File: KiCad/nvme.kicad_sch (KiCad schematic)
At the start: 35 parts, among them J10 Bus_M.2_Socket_M, J11 Bus_M.2_Socket_M, J12 Bus_M.2_Socket_M, J13 Bus_M.2_Socket_M, J14 Bus_M.2_Socket_M

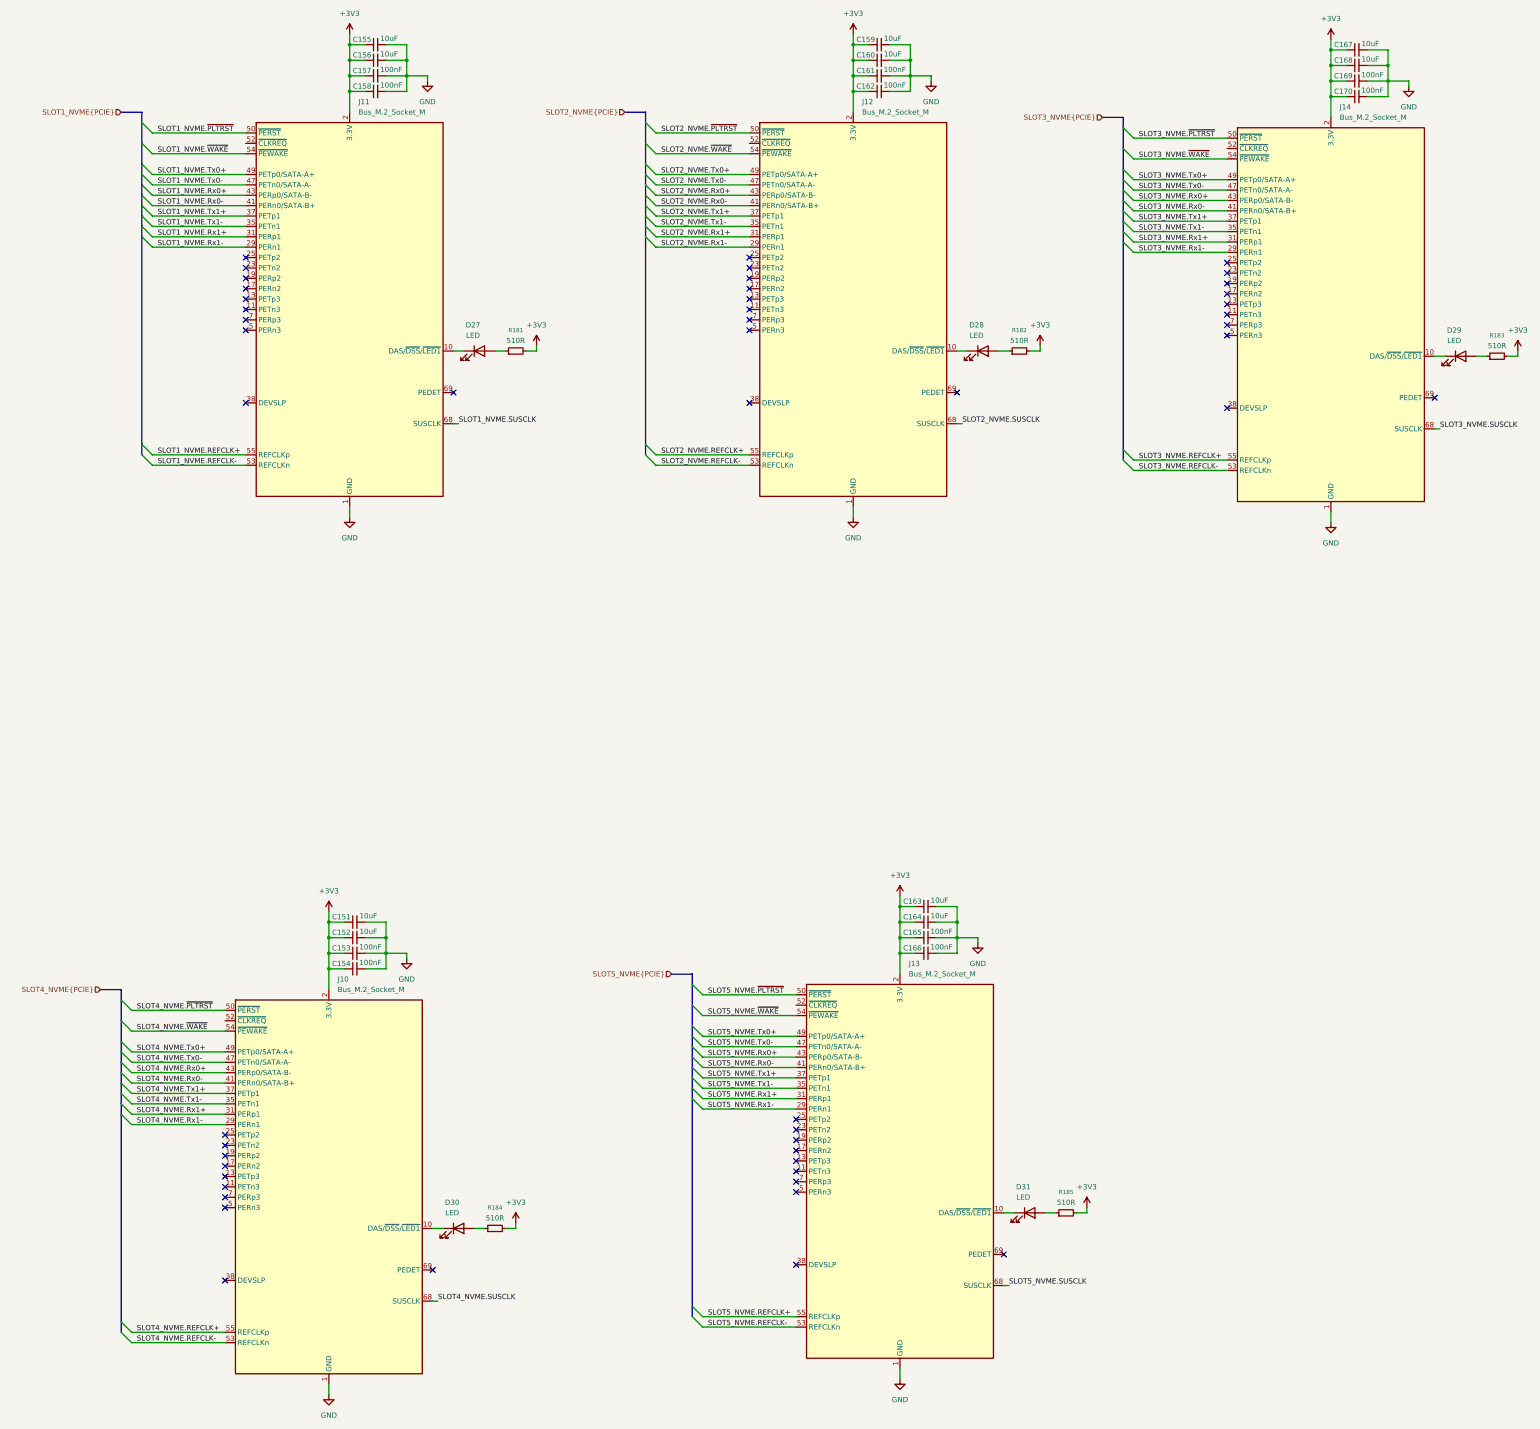
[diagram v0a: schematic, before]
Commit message: Remove 0.95V Power Supply, Replace 3.3V Standby Power Supply
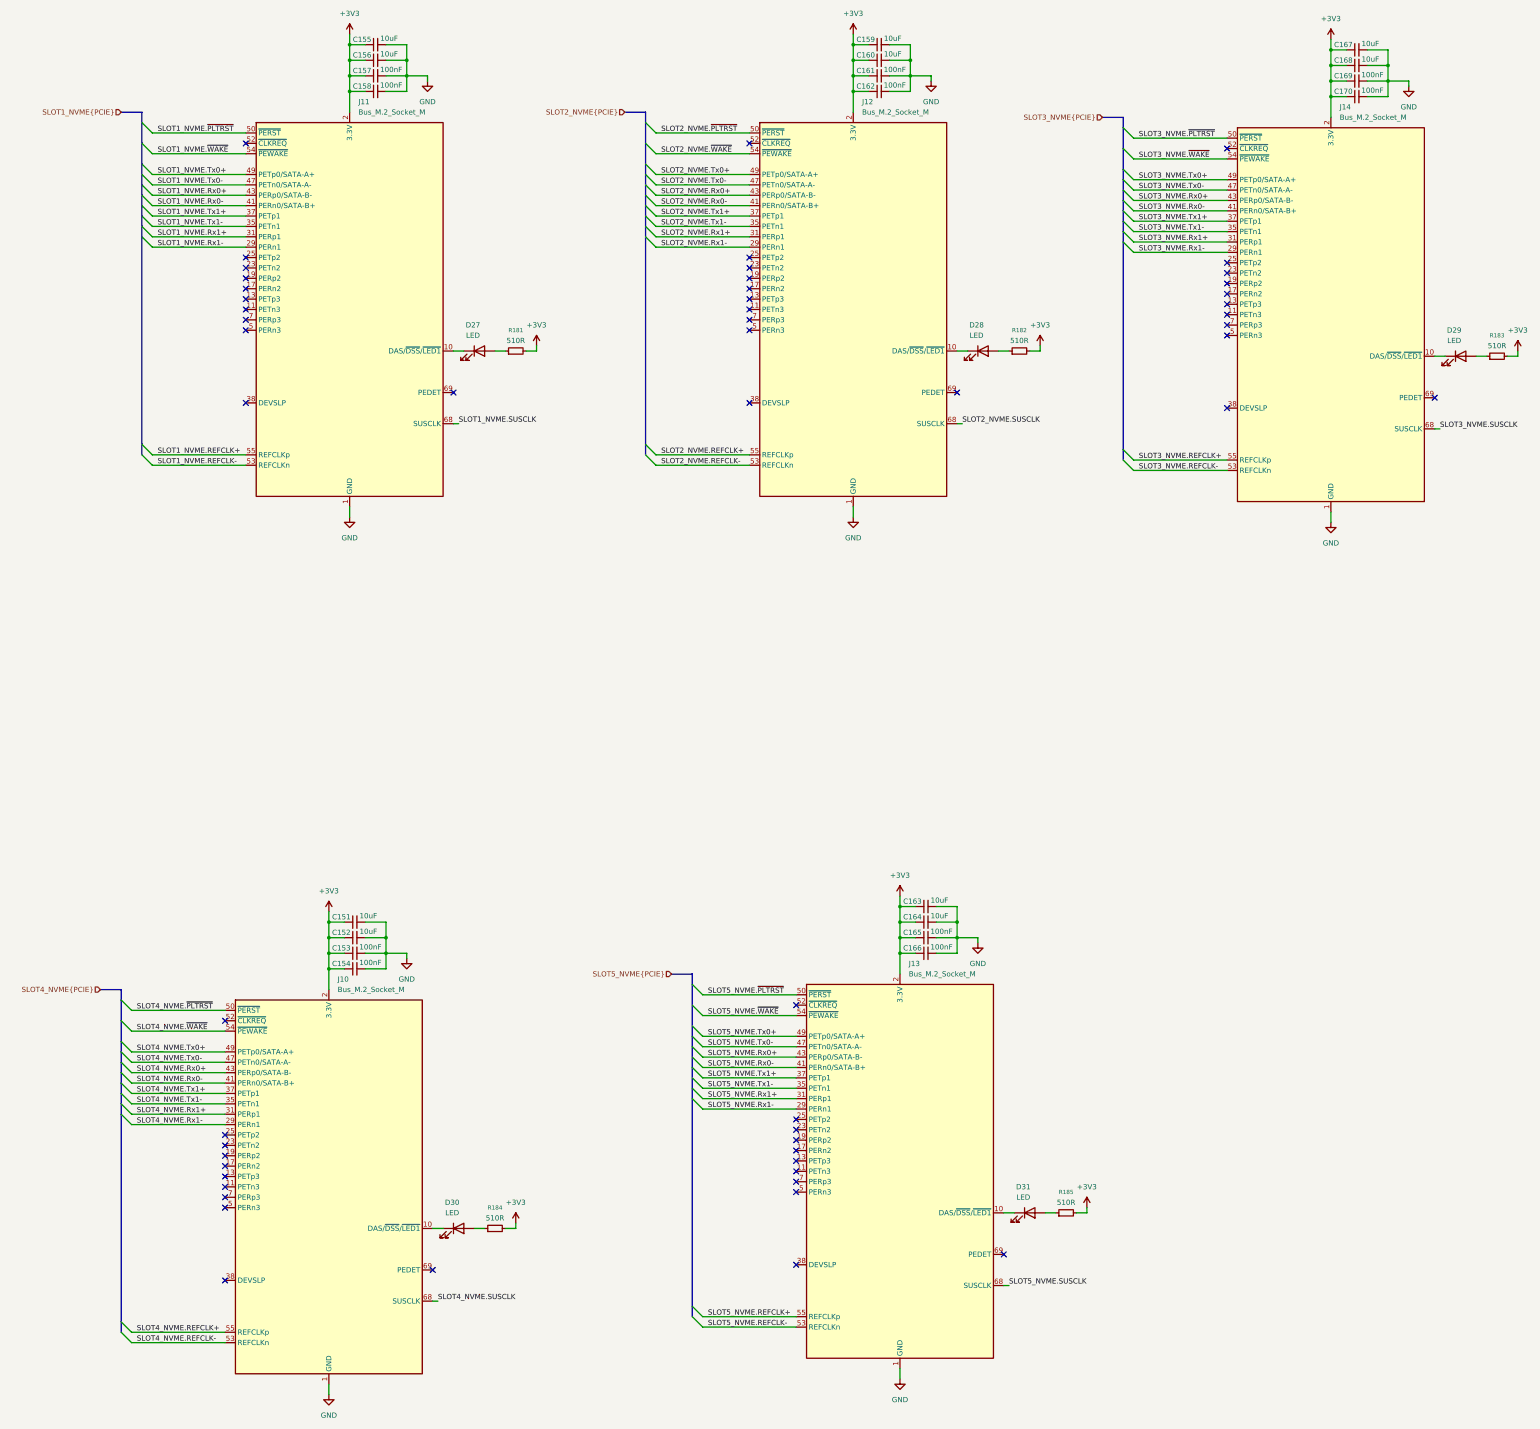
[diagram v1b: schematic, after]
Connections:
- no-connect marks 50 -> 55
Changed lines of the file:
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@@
+	)
+	(no_connect
+		(at 132.08 60.96)
 	)
 	(no_connect
@@
 	(no_connect
 		(at 127 321.31)
+	)
+	(no_connect
+		(at 255.27 60.96)
 	)
 	(no_connect
@@
 	(no_connect
 		(at 132.08 101.6)
+	)
+	(no_connect
+		(at 266.7 271.78)
 	)
 	(no_connect
@@
 	)
 	(no_connect
+		(at 372.11 62.23)
+	)
+	(no_connect
 		(at 255.27 106.68)
 	)
@@
 	)
 	(no_connect
+		(at 127 275.59)
+	)
+	(no_connect

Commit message: Work though ERC errors
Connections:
- net SLOT2_NVME.REFCLK+: now also J10.55 (REFCLKp); no longer J12.55 (REFCLKp)
- net SLOT2_NVME.REFCLK-: now also J10.53 (REFCLKn); no longer J12.53 (REFCLKn)
- net SLOT2_NVME.Rx0+: now also J10.43 (PERp0/SATA-B-); no longer J12.43 (PERp0/SATA-B-)
- net SLOT2_NVME.Rx0-: now also J10.41 (PERn0/SATA-B+); no longer J12.41 (PERn0/SATA-B+)
- net SLOT2_NVME.Rx1+: now also J10.31 (PERp1); no longer J12.31 (PERp1)
- net SLOT2_NVME.Rx1-: now also J10.29 (PERn1); no longer J12.29 (PERn1)
- net SLOT2_NVME.SUSCLK: now also J10.68 (SUSCLK); no longer J12.68 (SUSCLK)
- net SLOT2_NVME.Tx0+: now also J10.49 (PETp0/SATA-A+); no longer J12.49 (PETp0/SATA-A+)
- net SLOT2_NVME.Tx0-: now also J10.47 (PETn0/SATA-A-); no longer J12.47 (PETn0/SATA-A-)
- net SLOT2_NVME.Tx1+: now also J10.37 (PETp1); no longer J12.37 (PETp1)
- net SLOT2_NVME.Tx1-: now also J10.35 (PETn1); no longer J12.35 (PETn1)
- net SLOT2_NVME.~{PLTRST}: now also J10.50 (~{PERST}); no longer J12.50 (~{PERST})
- net SLOT2_NVME.~{WAKE}: now also J10.54 (~{PEWAKE}); no longer J12.54 (~{PEWAKE})
- net SLOT3_NVME.REFCLK+: now also J12.55 (REFCLKp); no longer J14.55 (REFCLKp)
- net SLOT3_NVME.REFCLK-: now also J12.53 (REFCLKn); no longer J14.53 (REFCLKn)
- net SLOT3_NVME.Rx0+: now also J12.43 (PERp0/SATA-B-); no longer J14.43 (PERp0/SATA-B-)
- net SLOT3_NVME.Rx0-: now also J12.41 (PERn0/SATA-B+); no longer J14.41 (PERn0/SATA-B+)
- net SLOT3_NVME.Rx1+: now also J12.31 (PERp1); no longer J14.31 (PERp1)
- net SLOT3_NVME.Rx1-: now also J12.29 (PERn1); no longer J14.29 (PERn1)
- net SLOT3_NVME.SUSCLK: now also J12.68 (SUSCLK); no longer J14.68 (SUSCLK)
- net SLOT3_NVME.Tx0+: now also J12.49 (PETp0/SATA-A+); no longer J14.49 (PETp0/SATA-A+)
- net SLOT3_NVME.Tx0-: now also J12.47 (PETn0/SATA-A-); no longer J14.47 (PETn0/SATA-A-)
- net SLOT3_NVME.Tx1+: now also J12.37 (PETp1); no longer J14.37 (PETp1)
- net SLOT3_NVME.Tx1-: now also J12.35 (PETn1); no longer J14.35 (PETn1)
- net SLOT3_NVME.~{PLTRST}: now also J12.50 (~{PERST}); no longer J14.50 (~{PERST})
- net SLOT3_NVME.~{WAKE}: now also J12.54 (~{PEWAKE}); no longer J14.54 (~{PEWAKE})
- net SLOT4_NVME.REFCLK+: now also J13.55 (REFCLKp); no longer J10.55 (REFCLKp)
- net SLOT4_NVME.REFCLK-: now also J13.53 (REFCLKn); no longer J10.53 (REFCLKn)
- net SLOT4_NVME.Rx0+: now also J13.43 (PERp0/SATA-B-); no longer J10.43 (PERp0/SATA-B-)
- net SLOT4_NVME.Rx0-: now also J13.41 (PERn0/SATA-B+); no longer J10.41 (PERn0/SATA-B+)
- net SLOT4_NVME.Rx1+: now also J13.31 (PERp1); no longer J10.31 (PERp1)
- net SLOT4_NVME.Rx1-: now also J13.29 (PERn1); no longer J10.29 (PERn1)
- net SLOT4_NVME.SUSCLK: now also J13.68 (SUSCLK); no longer J10.68 (SUSCLK)
- net SLOT4_NVME.Tx0+: now also J13.49 (PETp0/SATA-A+); no longer J10.49 (PETp0/SATA-A+)
- net SLOT4_NVME.Tx0-: now also J13.47 (PETn0/SATA-A-); no longer J10.47 (PETn0/SATA-A-)
- net SLOT4_NVME.Tx1+: now also J13.37 (PETp1); no longer J10.37 (PETp1)
- net SLOT4_NVME.Tx1-: now also J13.35 (PETn1); no longer J10.35 (PETn1)
- net SLOT4_NVME.~{PLTRST}: now also J13.50 (~{PERST}); no longer J10.50 (~{PERST})
- net SLOT4_NVME.~{WAKE}: now also J13.54 (~{PEWAKE}); no longer J10.54 (~{PEWAKE})
- net SLOT5_NVME.REFCLK+: now also J14.55 (REFCLKp); no longer J13.55 (REFCLKp)
- net SLOT5_NVME.REFCLK-: now also J14.53 (REFCLKn); no longer J13.53 (REFCLKn)
- net SLOT5_NVME.Rx0+: now also J14.43 (PERp0/SATA-B-); no longer J13.43 (PERp0/SATA-B-)
- net SLOT5_NVME.Rx0-: now also J14.41 (PERn0/SATA-B+); no longer J13.41 (PERn0/SATA-B+)
- net SLOT5_NVME.Rx1+: now also J14.31 (PERp1); no longer J13.31 (PERp1)
- net SLOT5_NVME.Rx1-: now also J14.29 (PERn1); no longer J13.29 (PERn1)
- net SLOT5_NVME.SUSCLK: now also J14.68 (SUSCLK); no longer J13.68 (SUSCLK)
- net SLOT5_NVME.Tx0+: now also J14.49 (PETp0/SATA-A+); no longer J13.49 (PETp0/SATA-A+)
- net SLOT5_NVME.Tx0-: now also J14.47 (PETn0/SATA-A-); no longer J13.47 (PETn0/SATA-A-)
- net SLOT5_NVME.Tx1+: now also J14.37 (PETp1); no longer J13.37 (PETp1)
- net SLOT5_NVME.Tx1-: now also J14.35 (PETn1); no longer J13.35 (PETn1)
- net SLOT5_NVME.~{PLTRST}: now also J14.50 (~{PERST}); no longer J13.50 (~{PERST})
- net SLOT5_NVME.~{WAKE}: now also J14.54 (~{PEWAKE}); no longer J13.54 (~{PEWAKE})
- net at D29.1 (K): now also J12.10 (DAS/~{DSS}/~{LED1}); no longer J14.10 (DAS/~{DSS}/~{LED1})
- net at D30.1 (K): now also J13.10 (DAS/~{DSS}/~{LED1}); no longer J10.10 (DAS/~{DSS}/~{LED1})
- net at D28.1 (K): now also J10.10 (DAS/~{DSS}/~{LED1}); no longer J12.10 (DAS/~{DSS}/~{LED1})
- net at D31.1 (K): now also J14.10 (DAS/~{DSS}/~{LED1}); no longer J13.10 (DAS/~{DSS}/~{LED1})

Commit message: Re-annotate components
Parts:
- renumbered C151 to C163, C152 to C164, C153 to C165, C154 to C166, C155 to C167, C156 to C168, C157 to C169, C158 to C170, C159 to C171, C160 to C172, C161 to C173, C162 to C174, C163 to C175, C164 to C176, C165 to C177, C166 to C178, C167 to C179, C168 to C180, C169 to C181, C170 to C182, D30 to D22, D27 to D23, D28 to D24, D31 to D25, D29 to D26, J13 to J10, J10 to J12, J14 to J13, J12 to J14, R184 to R108, R181 to R109, R182 to R110, R185 to R111, R183 to R112

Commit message: Add more footprints
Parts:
- C163, C164, C165, C166, C167, C168, C169, C170, C171, C172, C173, C174, C175, C176, C177, C178, C179, C180, C181, C182: footprint (none) -> Capacitor_SMD:C_0603_1608Metric
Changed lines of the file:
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@@
 			)
 		)
-		(property "Footprint" ""
+		(property "Footprint" "Capacitor_SMD:C_0603_1608Metric"
 			(at 298.45 259.08 0)
 			(effects
@@
 			)
 		)
-		(property "Footprint" ""
+		(property "Footprint" "Capacitor_SMD:C_0603_1608Metric"
 			(at 158.75 259.08 0)
 			(effects
@@
 			)
 		)
-		(property "Footprint" ""
+		(property "Footprint" "Capacitor_SMD:C_0603_1608Metric"
 			(at 158.75 255.27 0)
 			(effects
@@
 			)
 		)
-		(property "Footprint" ""
+		(property "Footprint" "Capacitor_SMD:C_0603_1608Metric"
 			(at 403.86 38.1 0)
 			(effects
@@
 			)
 		)
-		(property "Footprint" ""
+		(property "Footprint" "Capacitor_SMD:C_0603_1608Metric"
 			(at 287.02 48.26 0)
 			(effects
@@
 			)
 		)
-		(property "Footprint" ""
+		(property "Footprint" "Capacitor_SMD:C_0603_1608Metric"
 			(at 163.83 36.83 0)
 			(effects
@@
 			)
 		)
-		(property "Footprint" ""
+		(property "Footprint" "Capacitor_SMD:C_0603_1608Metric"
 			(at 158.75 251.46 0)
 			(effects
@@
 			)
 		)
-		(property "Footprint" ""
+		(property "Footprint" "Capacitor_SMD:C_0603_1608Metric"
 			(at 163.83 48.26 0)
 			(effects
@@
 			)
 		)
-		(property "Footprint" ""
+		(property "Footprint" "Capacitor_SMD:C_0603_1608Metric"
 			(at 298.45 255.27 0)
 			(effects
@@
 			)
 		)
-		(property "Footprint" ""
+		(property "Footprint" "Capacitor_SMD:C_0603_1608Metric"
 			(at 287.02 36.83 0)
 			(effects
@@
 			)
 		)
-		(property "Footprint" ""
+		(property "Footprint" "Capacitor_SMD:C_0603_1608Metric"
 			(at 163.83 44.45 0)
 			(effects
@@
 			)
 		)
-		(property "Footprint" ""
+		(property "Footprint" "Capacitor_SMD:C_0603_1608Metric"
 			(at 287.02 44.45 0)
 			(effects
@@
 			)
 		)
-		(property "Footprint" ""
+		(property "Footprint" "Capacitor_SMD:C_0603_1608Metric"
 			(at 403.86 49.53 0)
 			(effects
@@
 			)
 		)
-		(property "Footprint" ""
+		(property "Footprint" "Capacitor_SMD:C_0603_1608Metric"
 			(at 403.86 41.91 0)
 			(effects
@@
 			)
 		)
-		(property "Footprint" ""
+		(property "Footprint" "Capacitor_SMD:C_0603_1608Metric"
 			(at 298.45 251.46 0)
 			(effects
@@
 			)
 		)
-		(property "Footprint" ""
+		(property "Footprint" "Capacitor_SMD:C_0603_1608Metric"
 			(at 403.86 45.72 0)
 			(effects
@@
 			)
 		)
-		(property "Footprint" ""
+		(property "Footprint" "Capacitor_SMD:C_0603_1608Metric"
 			(at 298.45 247.65 0)
 			(effects
@@
 			)
 		)
-		(property "Footprint" ""
+		(property "Footprint" "Capacitor_SMD:C_0603_1608Metric"
 			(at 158.75 262.89 0)
 			(effects
@@
 			)
 		)
-		(property "Footprint" ""
+		(property "Footprint" "Capacitor_SMD:C_0603_1608Metric"
 			(at 163.83 40.64 0)
 			(effects
@@
 			)
 		)
-		(property "Footprint" ""
+		(property "Footprint" "Capacitor_SMD:C_0603_1608Metric"
 			(at 287.02 40.64 0)
 			(effects
